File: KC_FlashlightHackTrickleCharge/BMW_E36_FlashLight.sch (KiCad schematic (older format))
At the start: 9 parts, among them J1 CONN_01X01_FEMALE, J2 CONN_01X01_FEMALE, SW1 SW_DIP_x01

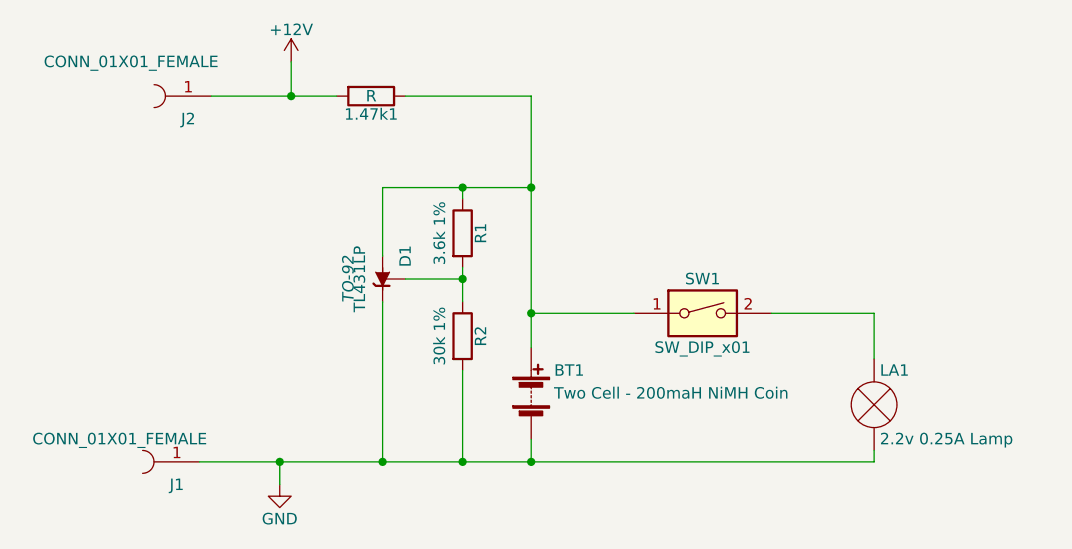
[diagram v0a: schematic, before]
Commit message: Adjusted the Treshold Voltage
Changed the threshold voltage from 2.8v to 2.75v
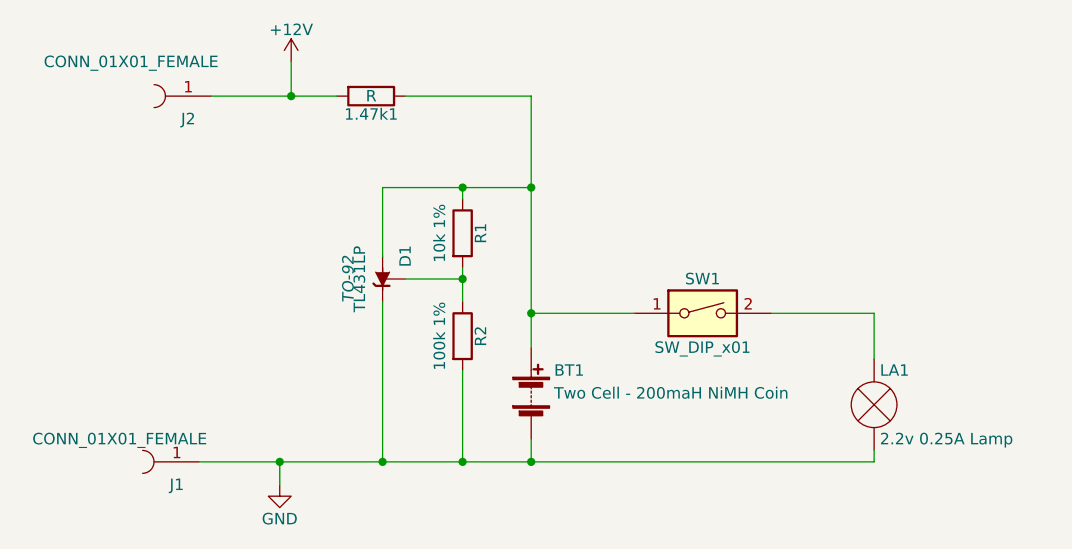
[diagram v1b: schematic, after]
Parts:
- R1: value 3.6k 1% -> 10k 1%
- R2: value 30k 1% -> 100k 1%
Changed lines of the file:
@@
 P 5000 3900
 F 0 "R1" V 5080 3900 50  0000 C CNN
-F 1 "3.6k 1%" V 4900 3900 50  0000 C CNN
+F 1 "10k 1%" V 4900 3900 50  0000 C CNN
 F 2 "" V 4930 3900 50  0000 C CNN
 F 3 "" H 5000 3900 50  0000 C CNN
@@
 P 5000 4350
 F 0 "R2" V 5080 4350 50  0000 C CNN
-F 1 "30k 1%" V 4900 4350 50  0000 C CNN
+F 1 "100k 1%" V 4900 4350 50  0000 C CNN
 F 2 "" V 4930 4350 50  0000 C CNN
 F 3 "" H 5000 4350 50  0000 C CNN

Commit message: Fixed the orientation of the TL431.  The anode and cathode were reversed, but now fixed.
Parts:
- SW1: symbol SW_DIP_x01 -> SW_DIP_x01-RESCUE-BMW_E36_FlashLight
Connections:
- net GND: now also D1.2 (A); no longer D1.3 (K)
- net at 1.47k1.1, BT1.1 (+), R1.1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: now also D1.3 (K); no longer D1.2 (A)
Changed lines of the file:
@@
 $EndComp
 $Comp
-L SW_DIP_x01 SW1
+L SW_DIP_x01-RESCUE-BMW_E36_FlashLight SW1
 U 1 1 59781418
 P 6050 4250
@@
 F 3 "" H 4650 4100 50  0000 C CNN
 	1    4650 4100
-	0    1    1    0
+	0    1    -1   0
 $EndComp
-Wire Wire Line
-	4650 4000 4650 3700
 Wire Wire Line
 	4650 3700 5300 3700
 Connection ~ 5300 3700
-Wire Wire Line
-	4650 4200 4650 4900
 Connection ~ 4650 4900
 $Comp
@@
 $EndComp
 Wire Wire Line
-	4750 4100 5000 4100
-Wire Wire Line
 	5000 4050 5000 4200
 Connection ~ 5000 4100
@@
 Wire Wire Line
 	4750 3300 5300 3300
+Wire Wire Line
+	4750 4100 5000 4100
+Wire Wire Line
+	4650 4000 4650 3700
+Wire Wire Line
+	4650 4200 4650 4900
 $EndSCHEMATC
